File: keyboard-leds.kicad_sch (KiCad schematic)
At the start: 53 parts, among them J1 USB_C_Receptacle_USB2.0_16P, J2 Conn_01x05, J4 Conn_01x03, J5 USB_C_Receptacle_USB2.0_16P, U1 RP2040, U10 TFT_320x240, U2 W25Q128JVS, U3 XC6206PxxxMR-Regulator_Linear, U5 TUSB320, U6 SN74AHCT1G125DBVR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

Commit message: Cleaned up footprints
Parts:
- U10: footprint ILI9341:TFT-320x240 -> ModHob:ILI9341_2.8in_Touch
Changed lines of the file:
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@@
 			)
 		)
-		(property "Footprint" "ILI9341:TFT-320x240"
+		(property "Footprint" "ModHob:ILI9341_2.8in_Touch"
 			(at 189.23 175.26 90)
 			(effects

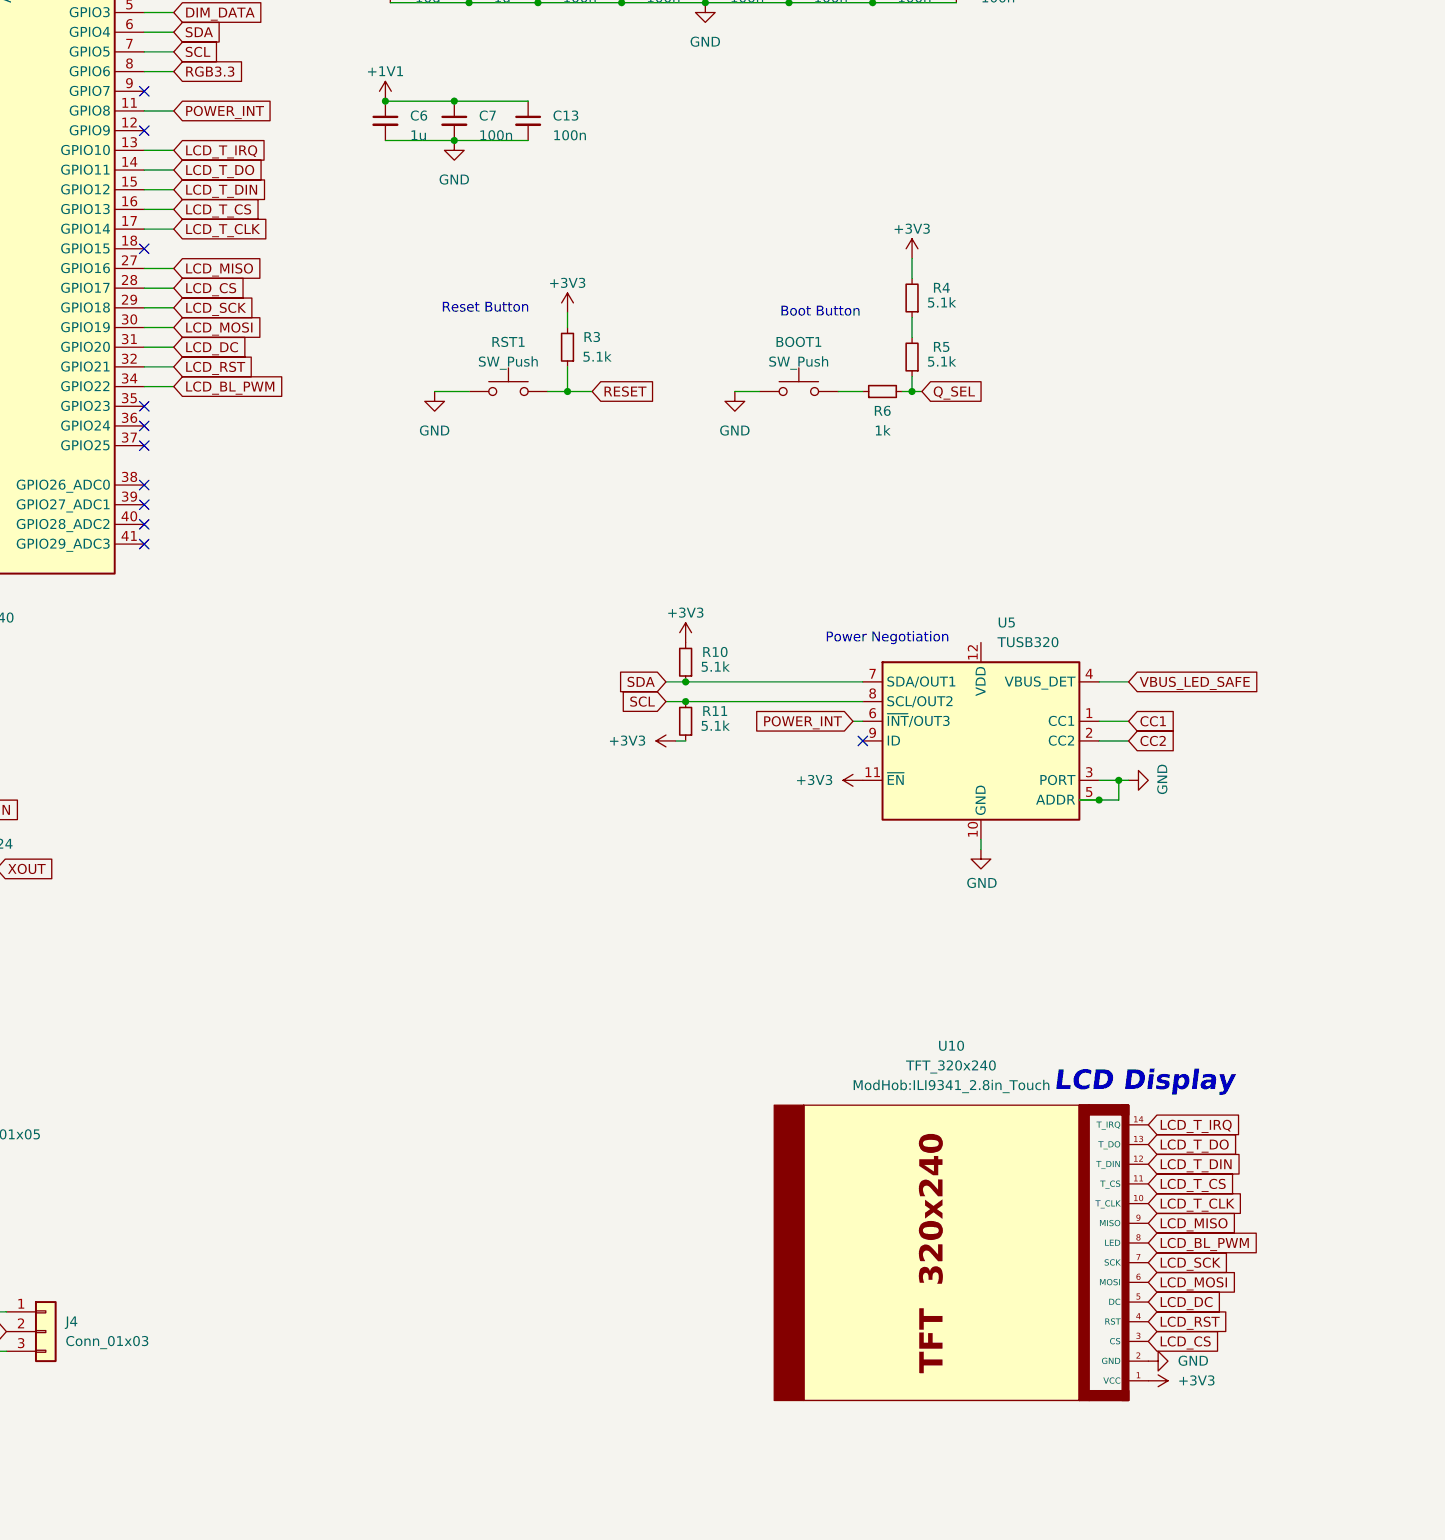
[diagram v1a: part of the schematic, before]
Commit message: Wired up SD Card, joined SPI devices
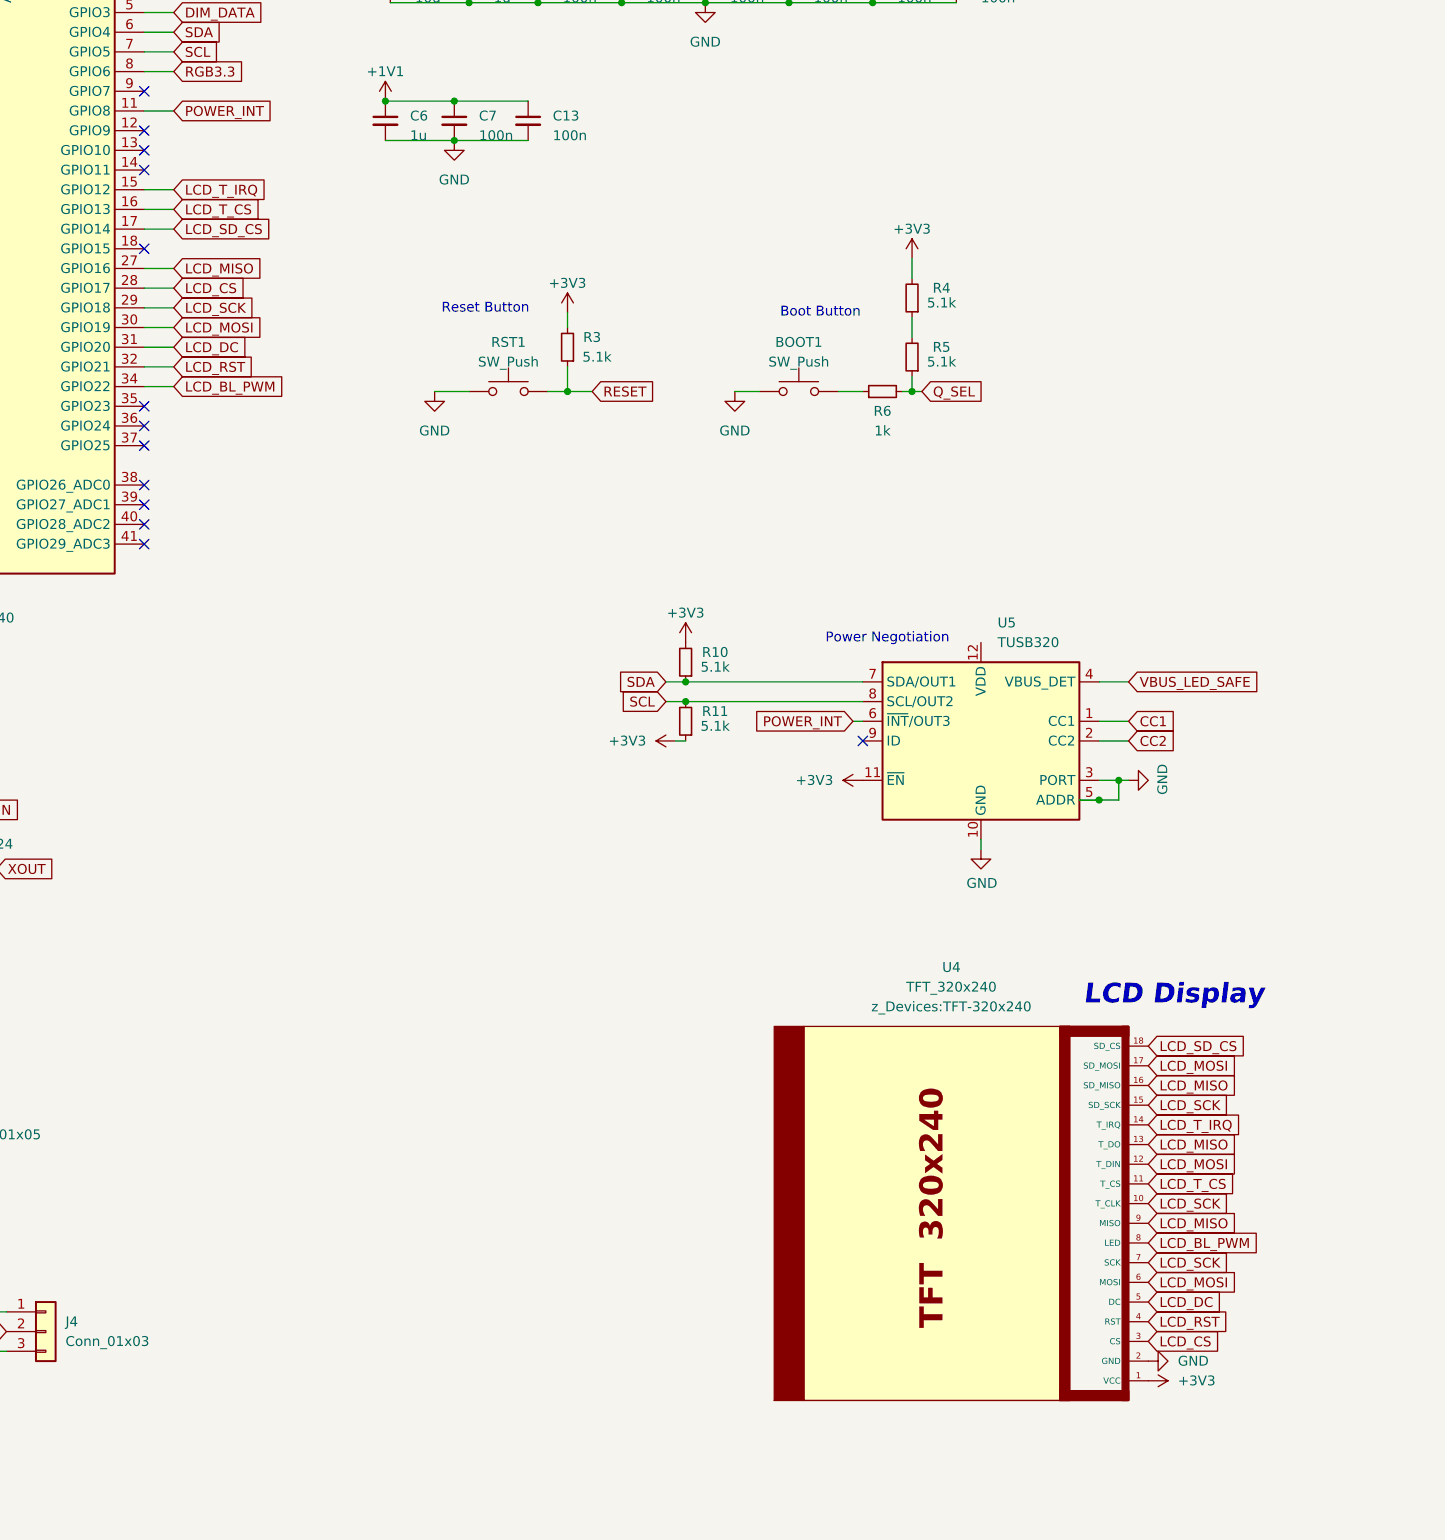
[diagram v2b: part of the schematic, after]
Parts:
- removed U10: TFT_320x240, ModHob:ILI9341_2.8in_Touch, symbol ILI9341:TFT_320x240
- added U4: TFT_320x240, z_Devices:TFT-320x240, symbol ModHob:TFT_320x240_SD
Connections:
- net LCD_T_DIN is gone; now on net LCD_T_IRQ: U1.15 (GPIO12)
- net +3V3: now also U4.1 (VCC)
- net GND: now also U4.2 (GND)
- net LCD_BL_PWM: now also U4.8 (LED)
- net LCD_CS: now also U4.3 (CS)
- net LCD_DC: now also U4.5 (DC)
- net LCD_MISO: now also U4.13 (T_DO), U4.16 (SD_MISO), U4.9 (MISO)
- net LCD_MOSI: now also U4.12 (T_DIN), U4.17 (SD_MOSI), U4.6 (MOSI)
- net LCD_RST: now also U4.4 (RST)
- net LCD_SCK: now also U4.10 (T_CLK), U4.15 (SD_SCK), U4.7 (SCK)
- net LCD_T_CS: now also U4.11 (T_CS)
- net LCD_T_IRQ: now also U4.14 (T_IRQ); no longer U1.13 (GPIO10)
- net LCD_T_CLK renamed LCD_SD_CS
- net LCD_SD_CS: now also U4.18 (SD_CS)
- net LCD_T_DO: no longer names the net of U1.14 (GPIO11)
- no-connect marks 25 -> 27

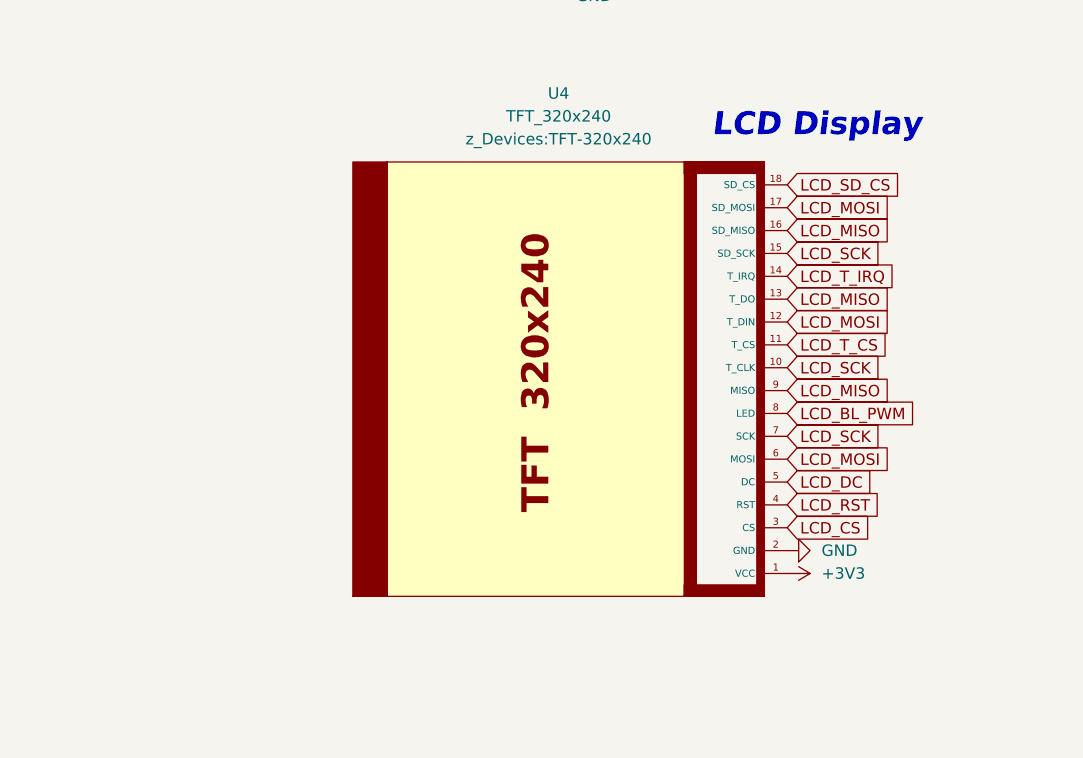
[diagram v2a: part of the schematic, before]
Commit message: Moved led output to other side for better cable management
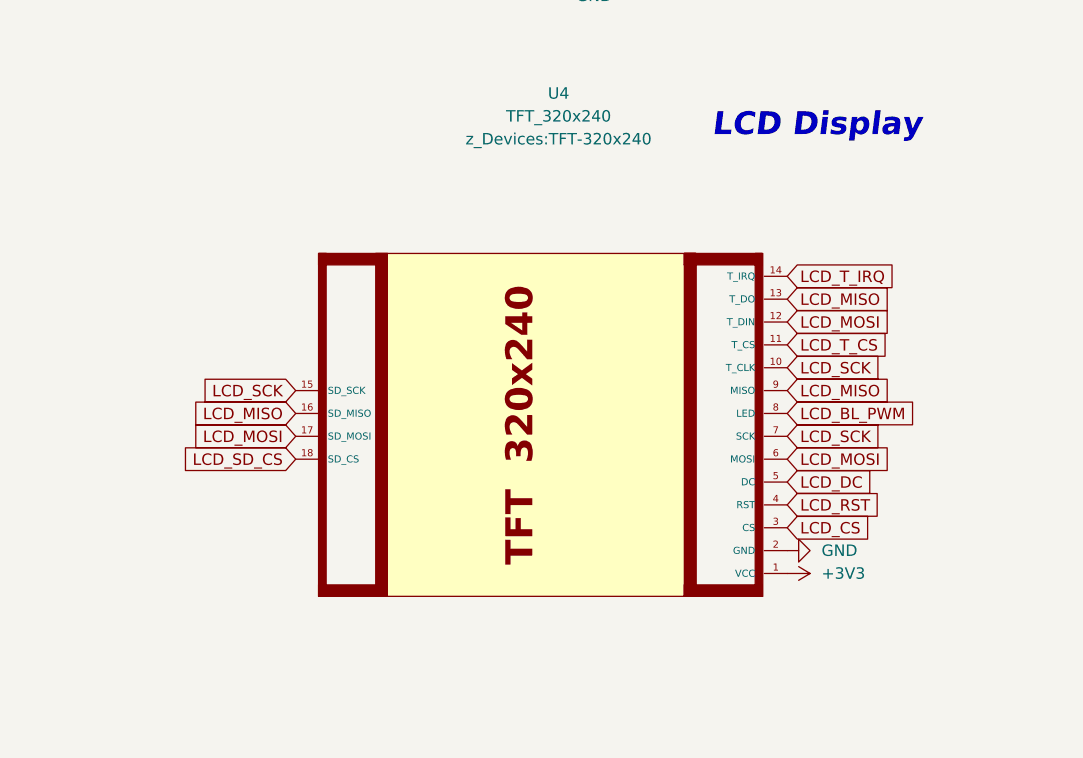
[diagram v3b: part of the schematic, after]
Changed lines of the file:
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@@
 	(global_label "LCD_SD_CS"
 		(shape input)
-		(at 214.63 170.18 0)
-		(effects
-			(font
-				(size 1.27 1.27)
-			)
-			(justify left)
-		)
-		(property "Intersheetrefs" "${INTERSHEET_REFS}"
-			(at 214.63 170.18 0)
+		(at 160.02 200.66 180)
+		(effects
+			(font
+				(size 1.27 1.27)
+			)
+			(justify right)
+		)
+		(property "Intersheetrefs" "${INTERSHEET_REFS}"
+			(at 160.02 200.66 0)
 			(effects
 				(font
@@
 	(global_label "LCD_MISO"
 		(shape input)
-		(at 214.63 175.26 0)
-		(fields_autoplaced yes)
-		(effects
-			(font
-				(size 1.27 1.27)
-			)
-			(justify left)
-		)
-		(property "Intersheetrefs" "${INTERSHEET_REFS}"
-			(at 226.7471 175.26 0)
-			(effects
-				(font
-					(size 1.27 1.27)
-				)
-				(justify left)
+		(at 160.02 195.58 180)
+		(fields_autoplaced yes)
+		(effects
+			(font
+				(size 1.27 1.27)
+			)
+			(justify right)
+		)
+		(property "Intersheetrefs" "${INTERSHEET_REFS}"
+			(at 147.9029 195.58 0)
+			(effects
+				(font
+					(size 1.27 1.27)
+				)
+				(justify right)
 				(hide yes)
 			)
@@
 	(global_label "LCD_SCK"
 		(shape input)
-		(at 214.63 177.8 0)
-		(fields_autoplaced yes)
-		(effects
-			(font
-				(size 1.27 1.27)
-			)
-			(justify left)
-		)
-		(property "Intersheetrefs" "${INTERSHEET_REFS}"
-			(at 225.9004 177.8 0)
-			(effects
-				(font
-					(size 1.27 1.27)
-				)
-				(justify left)
+		(at 160.02 193.04 180)
+		(fields_autoplaced yes)
+		(effects
+			(font
+				(size 1.27 1.27)
+			)
+			(justify right)
+		)
+		(property "Intersheetrefs" "${INTERSHEET_REFS}"
+			(at 148.7496 193.04 0)
+			(effects
+				(font
+					(size 1.27 1.27)
+				)
+				(justify right)
 				(hide yes)
 			)
@@
 	(global_label "LCD_MOSI"
 		(shape input)
-		(at 214.63 172.72 0)
-		(fields_autoplaced yes)
-		(effects
-			(font
-				(size 1.27 1.27)
-			)
-			(justify left)
-		)
-		(property "Intersheetrefs" "${INTERSHEET_REFS}"
-			(at 226.7471 172.72 0)
-			(effects
-				(font
-					(size 1.27 1.27)
-				)
-				(justify left)
-				(hide yes)
-			)
+		(at 160.02 198.12 180)
+		(fields_autoplaced yes)
+		(effects
+			(font
+				(size 1.27 1.27)
+			)
+			(justify right)
+		)
+		(property "Intersheetrefs" "${INTERSHEET_REFS}"
+			(at 147.9029 198.12 0)
+			(effects
+				(font
+					(size 1.27 1.27)
+				)
+				(justify right)
+				(hide yes)
+			)

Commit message: Cleaned up footprints
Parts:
- J1, J5: footprint PCM_marbastlib-various:USB_C_Receptacle_HRO_TYPE-C-31-M-12 -> ModHob:USB_C_Receptacle_HRO_TYPE-C-31-M-12
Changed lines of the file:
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@@
 			)
 		)
-		(property "Footprint" "PCM_marbastlib-various:USB_C_Receptacle_HRO_TYPE-C-31-M-12"
+		(property "Footprint" "ModHob:USB_C_Receptacle_HRO_TYPE-C-31-M-12"
 			(at 302.26 119.38 0)
 			(effects
@@
 			)
 		)
-		(property "Footprint" "PCM_marbastlib-various:USB_C_Receptacle_HRO_TYPE-C-31-M-12"
+		(property "Footprint" "ModHob:USB_C_Receptacle_HRO_TYPE-C-31-M-12"
 			(at 302.26 48.26 0)
 			(effects
